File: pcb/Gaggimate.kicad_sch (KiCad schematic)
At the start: 67 parts, among them J1 USB_C_Receptacle, J10 Conn_01x02, J2 Conn_01x02, J3 Conn_01x03, J4 Conn_01x04, J5 Conn_01x05, J6 Conn_01x10, J7 Conn_01x02, J8 Conn_01x02, J9 Conn_01x04, K1 Relay_SPDT, K2 Relay_SPDT, K3 Relay_SPDT, Q1 MMBT2222A, Q2 MMBT2222A, Q3 MMBT2222A, SW1 SW_Push, SW2 SW_Push, U1 ESP32-S3-WROOM-1, U2 AMS1117-3.3, U3 USBLC6-2SC6, U6 MAX31855EASA

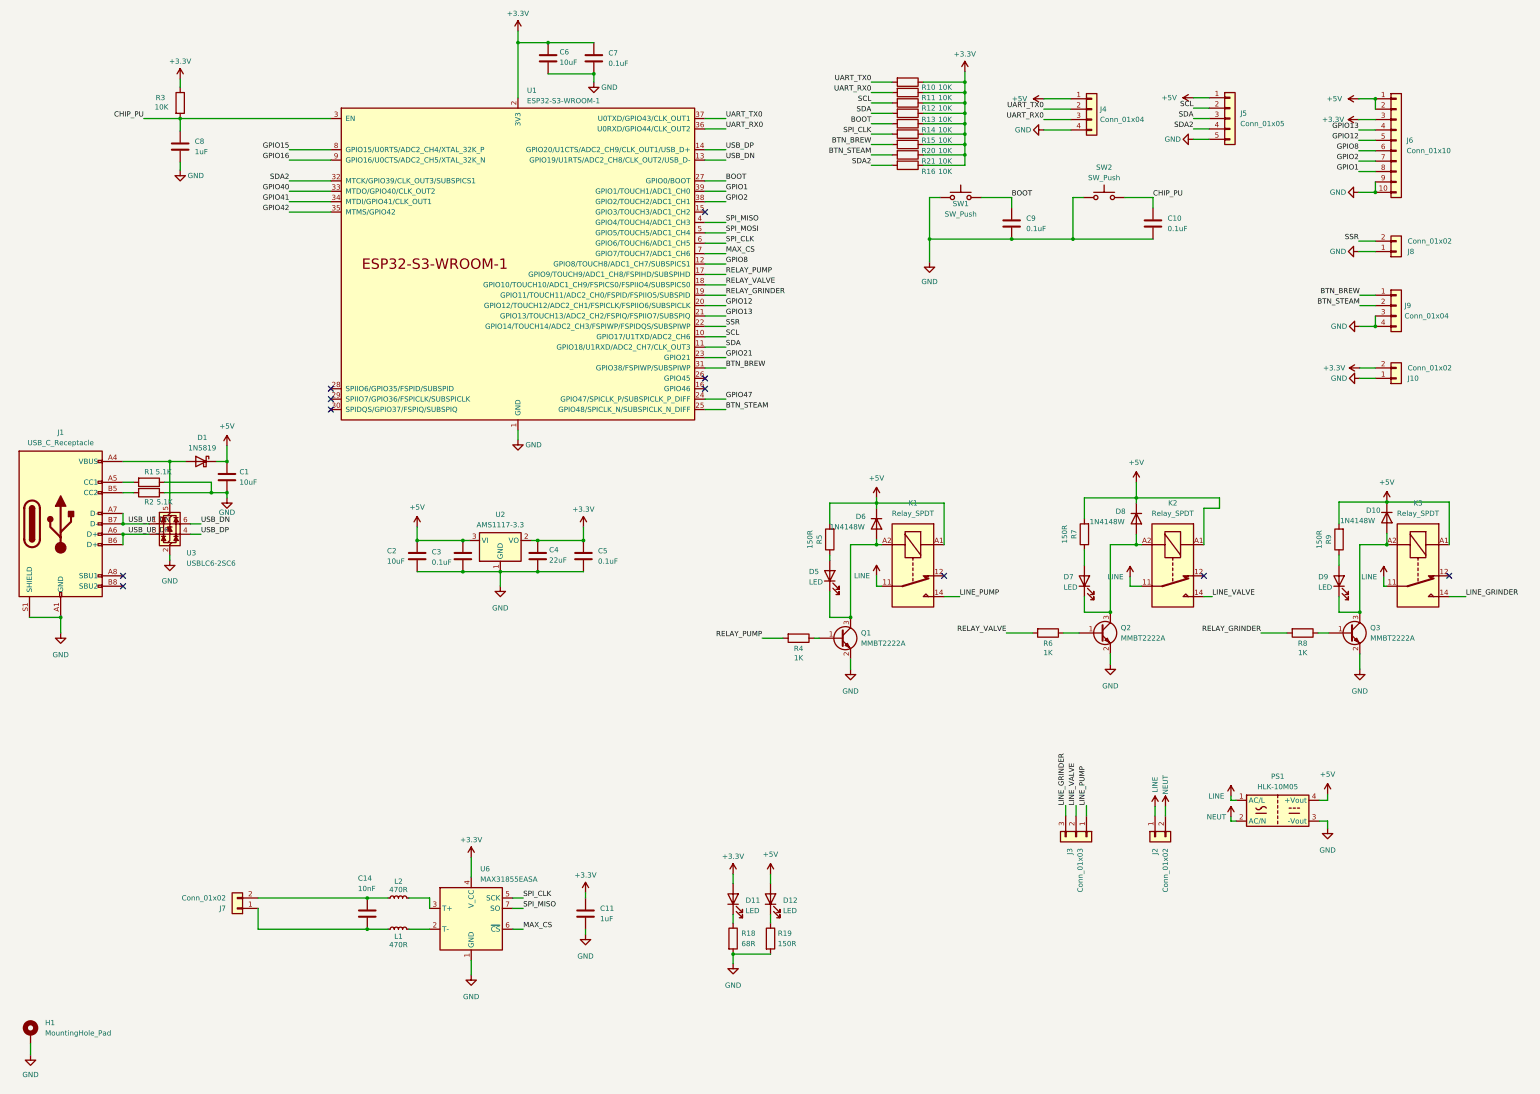
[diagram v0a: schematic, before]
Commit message: Add new variant for pcb gen 2
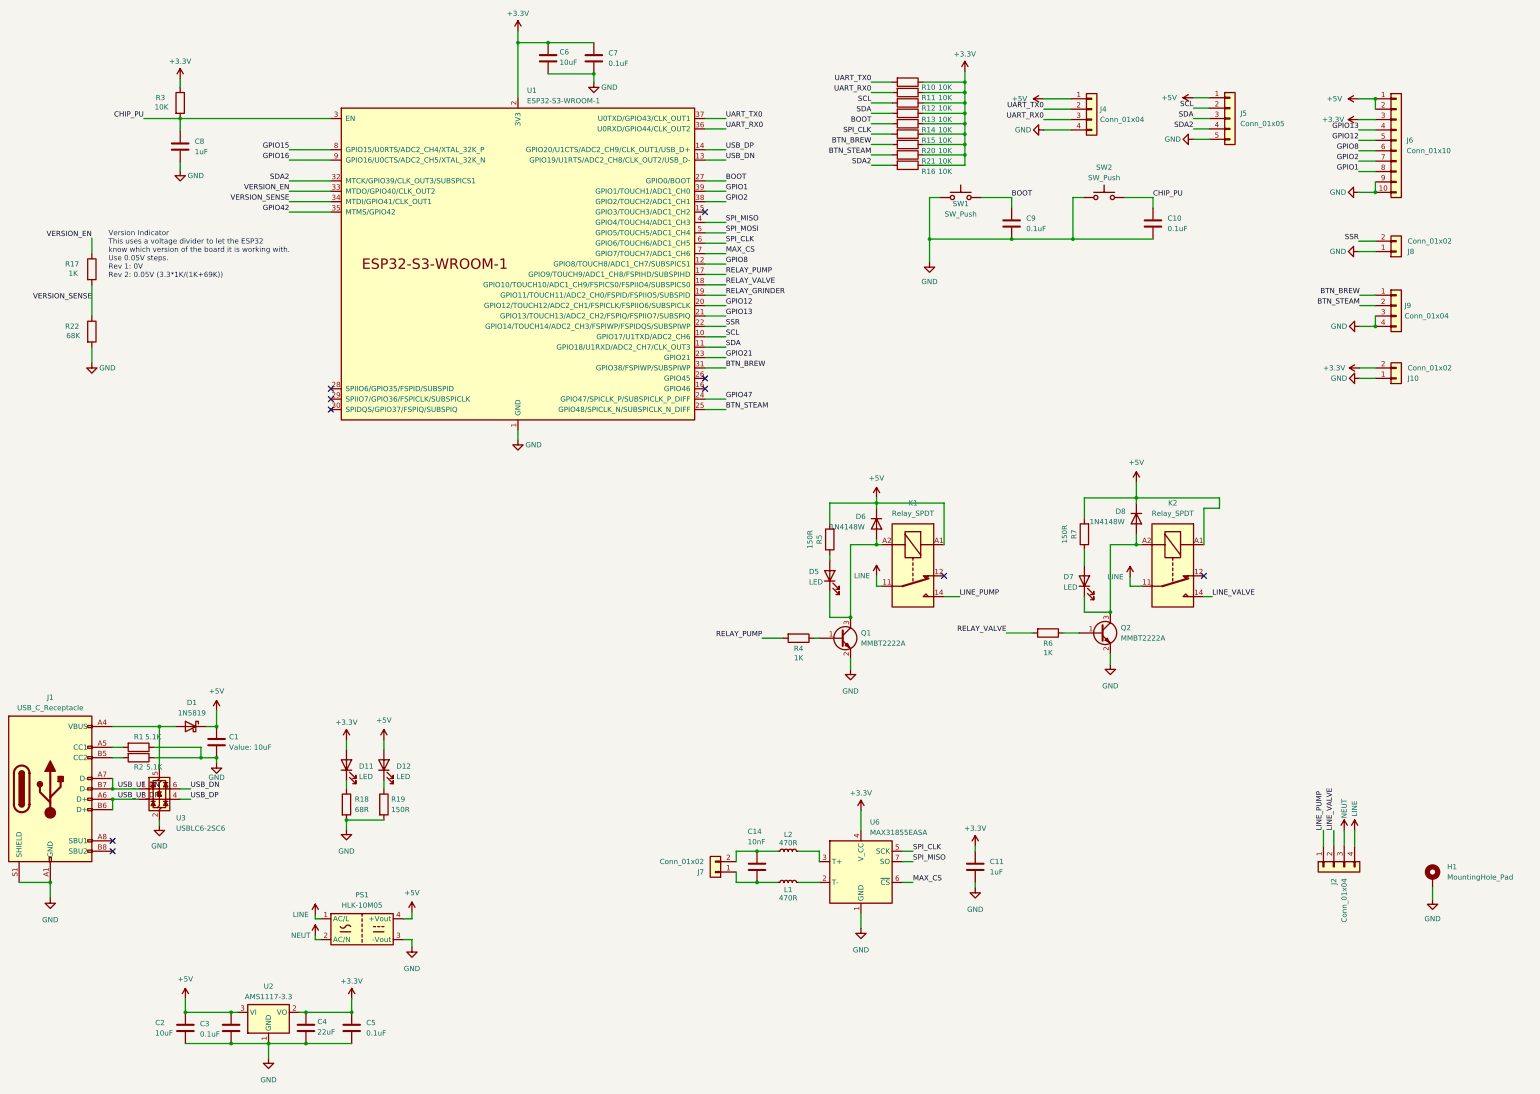
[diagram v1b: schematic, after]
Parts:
- removed D10: 1N4148W, Diode_SMD:D_SOD-123, symbol Device:D
- removed D9: LED, LED_SMD:LED_0805_2012Metric, symbol Device:LED
- removed J3: Conn_01x03, TerminalBlock:TerminalBlock_bornier-3_P5.08mm, symbol Connector_Generic:Conn_01x03
- removed K3: Relay_SPDT, Relay_THT:Relay_SPDT_Finder_36.11, symbol Relay:Relay_SPDT
- removed Q3: MMBT2222A, Package_TO_SOT_SMD:SOT-23, symbol Transistor_BJT:MMBT2222A
- removed R8: 1K, Resistor_SMD:R_0805_2012Metric, symbol Device:R
- removed R9: 150R, Resistor_SMD:R_0805_2012Metric, symbol Device:R
- added R17: 1K, Resistor_SMD:R_0402_1005Metric, symbol Device:R
- added R22: 68K, Resistor_SMD:R_0402_1005Metric, symbol Device:R
- C1, C10, C11, C14, C2, C3, C4, C5, C6, C7, C8, C9: footprint Capacitor_SMD:C_0805_2012Metric -> Capacitor_SMD:C_0402_1005Metric
- J10, J8: footprint Connector_JST:JST_XH_B2B-XH-A_1x02_P2.50mm_Vertical -> Connector_JST:JST_PH_B2B-PH-K_1x02_P2.00mm_Vertical
- J2: value Conn_01x02 -> Conn_01x04; footprint TerminalBlock:TerminalBlock_bornier-2_P5.08mm -> TerminalBlock:TerminalBlock_bornier-4_P5.08mm; symbol Connector_Generic:Conn_01x02 -> Connector_Generic:Conn_01x04
- J4, J9: footprint Connector_JST:JST_XH_B4B-XH-A_1x04_P2.50mm_Vertical -> Connector_JST:JST_PH_B4B-PH-K_1x04_P2.00mm_Vertical
- J5: footprint Connector_JST:JST_XH_B5B-XH-A_1x05_P2.50mm_Vertical -> Connector_JST:JST_PH_B5B-PH-K_1x05_P2.00mm_Vertical
- R1, R10, R11, R12, R13, R14, R15, R16, R18, R19, R2, R20, R21, R3, R4, R5, R6, R7: footprint Resistor_SMD:R_0805_2012Metric -> Resistor_SMD:R_0402_1005Metric
- SW1, SW2: footprint Button_Switch_SMD:SW_SPST_SKQG_WithStem -> Button_Switch_SMD:SW_SPST_B3U-3100P-B
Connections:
- net GND: now also R22.2
- net LINE: now also J2.4 (Pin_4); no longer J2.1 (Pin_1)
- net LINE_PUMP: now also J2.1 (Pin_1)
- net LINE_VALVE: now also J2.2 (Pin_2)
- net NEUT: now also J2.3 (Pin_3); no longer J2.2 (Pin_2)
- net GPIO40 renamed VERSION_EN
- net VERSION_EN: now also R17.1
- net GPIO41 renamed VERSION_SENSE
- net VERSION_SENSE: now also R17.2, R22.1
- no-connect marks 11 -> 10
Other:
- note added: "Version Indicator This uses a voltage divider to let the ESP32 know which version of the board it is working with. Use 0.05V steps. Rev 1: 0V Rev 2: 0.05V (3.3*1K/(1K+69K))"
- moved on the sheet: C1, C11, C14, C2, C3, C4, C5, D1, D11, D12, H1, J1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
